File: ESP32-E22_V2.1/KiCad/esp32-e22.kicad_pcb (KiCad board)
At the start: 2 copper layers, 69.9 x 97.8 mm, 36 parts, among them J1 Conn_01x04_Socket, J10 Conn_01x02_Socket, J3 Conn_01x04_Socket, J4 Conn_01x03_Socket, J5 SMA, J6 Conn_01x02_Socket, J7 USB_C_Receptacle_PowerOnly_6P, J8 Conn_01x04_Socket, J9 Conn_01x02_Socket, SW1 SW_Push, U1 E22-40033S, U2 ESP32-DevKitC, U3 DM-OLED096-636

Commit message: new Version 2.0.10 & 2.0.6
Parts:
- removed J7: USB_C_Receptacle_PowerOnly_6P, Connector_USB:USB_C_Receptacle_GCT_USB4125-xx-x-0190_6P_TopMnt_Horizontal
- added J2: Conn_01x04_Socket, Connector_PinHeader_2.54mm:PinHeader_1x04_P2.54mm_Vertical, F.Cu at (158.8, 130.8)
- moved J8 47.4 mm to (123.2, 77.5), turned to 180 degrees
- moved D1 2.54 mm to (166.4, 119.4)
- moved R7 1.27 mm to (162.6, 104.1)
- moved R6 0.63 mm to (162.6, 107.3)
- moved REF** 0.32 mm to (175.6, 63.4)
- moved REF** 0.31 mm to (175.6, 138.4)
- moved REF** 0.07 mm to (115.6, 63.4)
- turned D2 to 180 degrees
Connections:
- D2 pad 1: GND -> +5V
- D2 pad 2: +5V -> GND
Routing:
- net /SDA: track 63.7 -> 121.9 mm
- net /SCL: track 57.0 -> 106.2 mm
- net +3.3V: track 135.9 -> 150.8 mm
- net Net-(D3-A): track 14.1 -> 4.87 mm
- net GND: track 417.2 -> 410.3 mm
- net +5V: track 113.6 -> 118.6 mm
- net Net-(J2-Pin_3): track 7.56 -> 8.83 mm
- net Net-(D1-A): track 7.62 -> 8.67 mm
- net /MISO: track 62.3 -> 63.1 mm
- net /E22_SCK: track 62.6 -> 63.3 mm
- net /E22_NSS: track 66.2 -> 66.9 mm
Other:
- board size 69.9 x 97.8 mm -> 70 x 99 mm

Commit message: real update
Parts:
- added C8: 100nF, Capacitor_THT:C_Disc_D4.7mm_W2.5mm_P5.00mm, F.Cu at (115.6, 75.0)
- added R8: 0R, Resistor_SMD:R_0805_2012Metric, B.Cu at (137.2, 55.4)
- J2: value Conn_01x04_Socket -> ~; footprint Connector_PinHeader_2.54mm:PinHeader_1x04_P2.54mm_Vertical -> footprints:USB-C_vert
- moved J2 3.17 mm to (161.9, 130.8), turned to 0 degrees
- moved D1 1.27 mm to (153.7, 125.7)
- renumbered C5 to C1, C6 to C2, C1 to C3, C2 to C4, C3 to C5, C7 to C6, C4 to C7, D3 to D1, D1 to D2, D2 to D3, J10 to J1, J9 to J3, J1 to J4, J4 to J5, J8 to J6, J3 to J7, J5 to J8, J6 to J9, R3 to R1, R4 to R2, R1 to R3, R2 to R4, U2 to U1, U3 to U2, U1 to U3
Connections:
- J8 pad 1: Net-(J5-In) -> Net-(J8-In)
- U3 pad 21: Net-(J5-In) -> Net-(U3-ANT)
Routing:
- net +3.3V: track 150.8 -> 159.5 mm
- net GND: track 410.3 -> 418.6 mm
- net /E22_DIO1: track 79.5 -> 72.8 mm
- net Net-(J5-In): track 6.64 -> 0.00 mm
- net /E22_BUSY: track 82.1 -> 76.9 mm
- net +5V: track 118.6 -> 122.4 mm
- net /E22_NRST: track 82.1 -> 78.4 mm
- net Net-(U3-ANT): track 0.00 -> 2.84 mm, vias 0 -> 1
- net Net-(J8-In): track 0.00 -> 2.39 mm
- net /MISO: track 63.1 -> 61.6 mm
- net Net-(D1-A): track 4.87 -> 5.87 mm
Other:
- board text added: "ESP32-E22 V2.1.0 designed by OE3WAS"

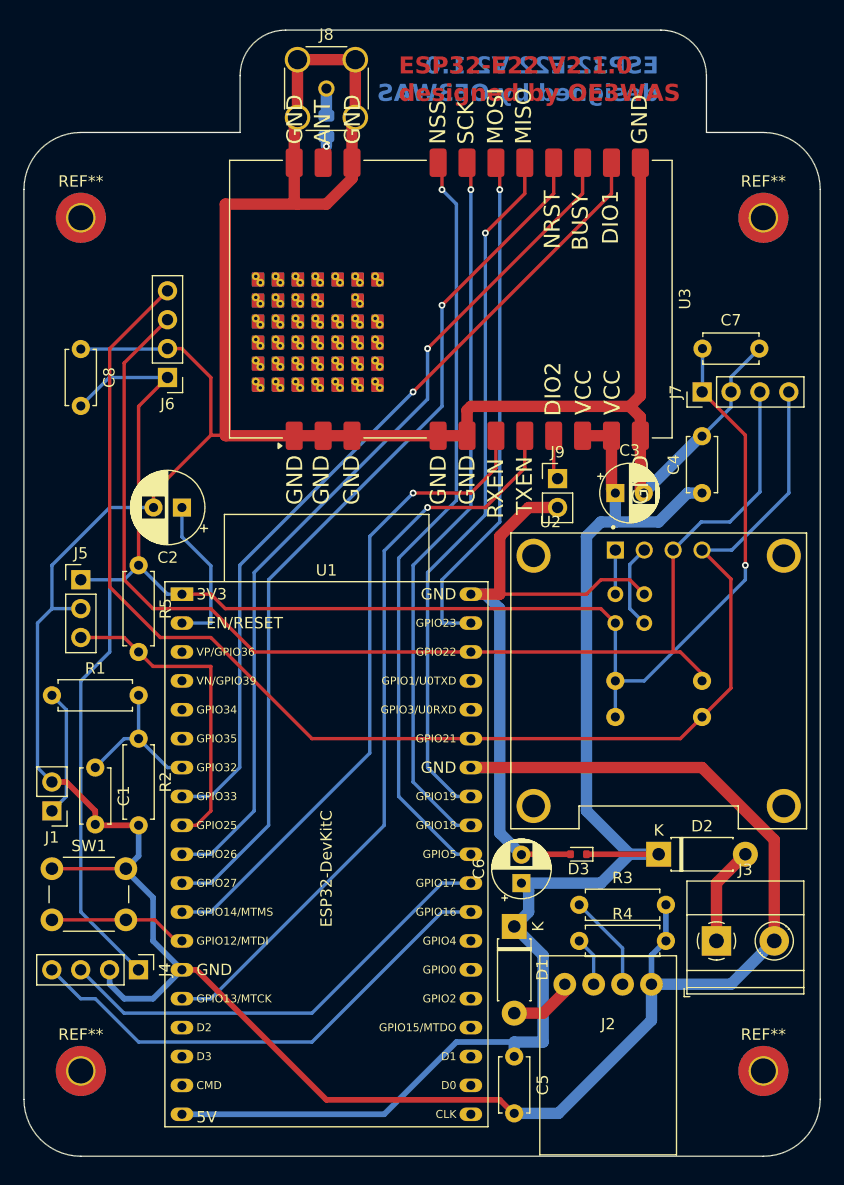
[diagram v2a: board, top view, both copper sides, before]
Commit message: Flood filled GND Back and Front
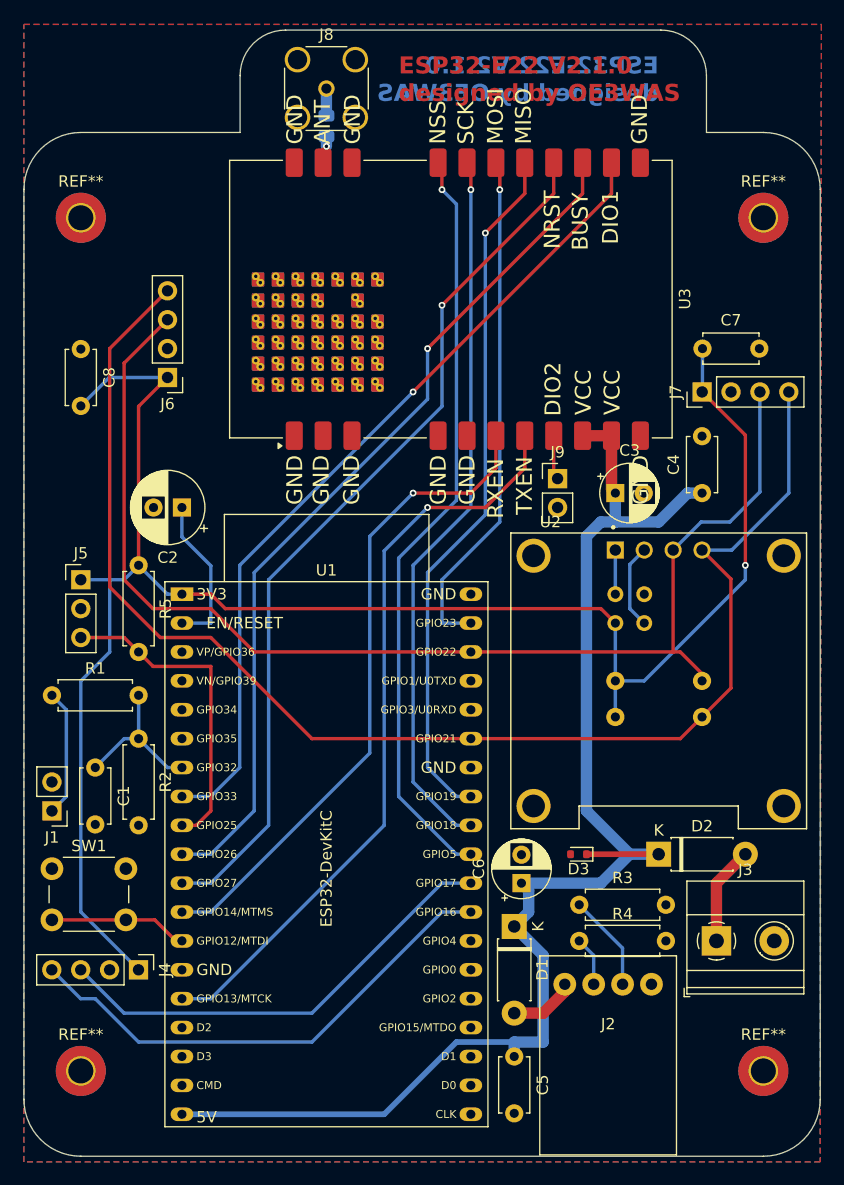
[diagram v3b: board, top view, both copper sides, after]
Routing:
- net GND: track 418.6 -> 0.00 mm
- added copper zone on B.Cu, net GND
- added copper zone on F.Cu, net GND

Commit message: some footprint changes
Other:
- board text added: "github.com/DK9BT/esp32-e22-lora-board"

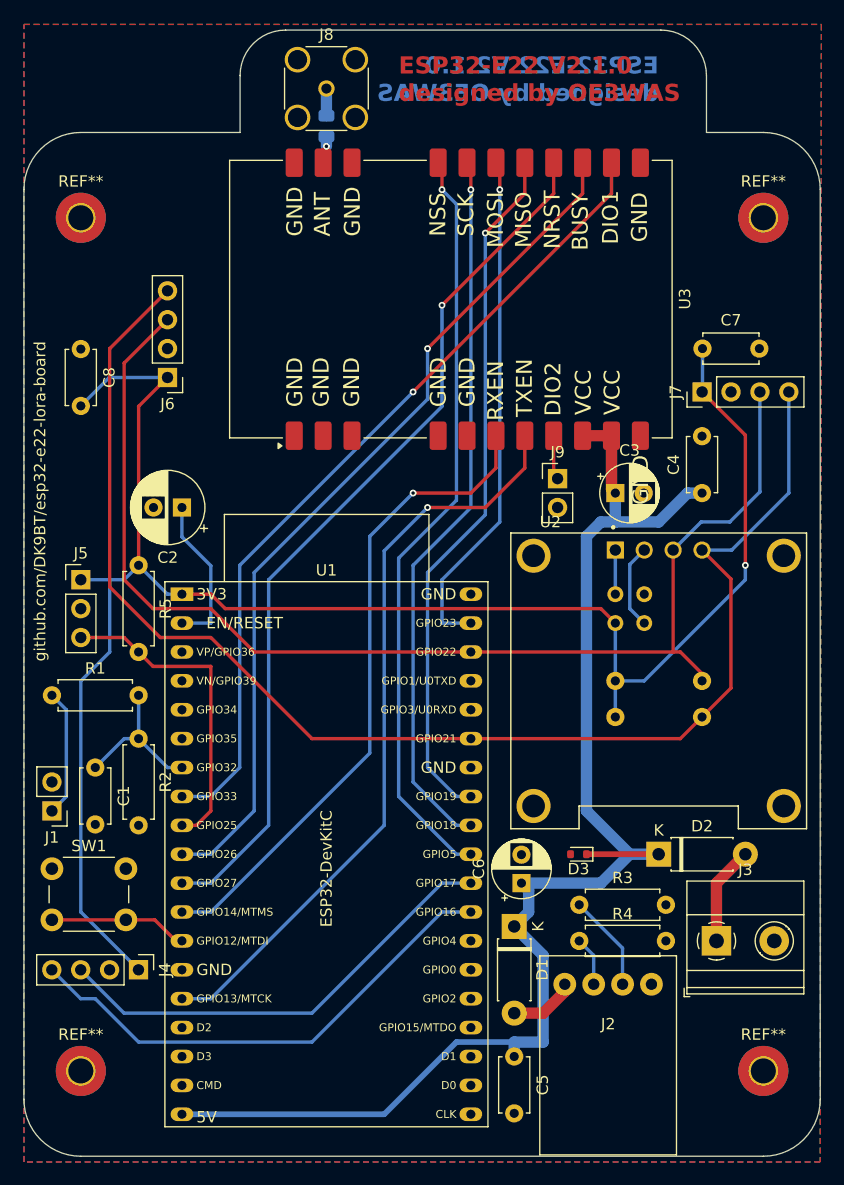
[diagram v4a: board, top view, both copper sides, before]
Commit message: corrected footprints symbols and 3d Models for our custom parts
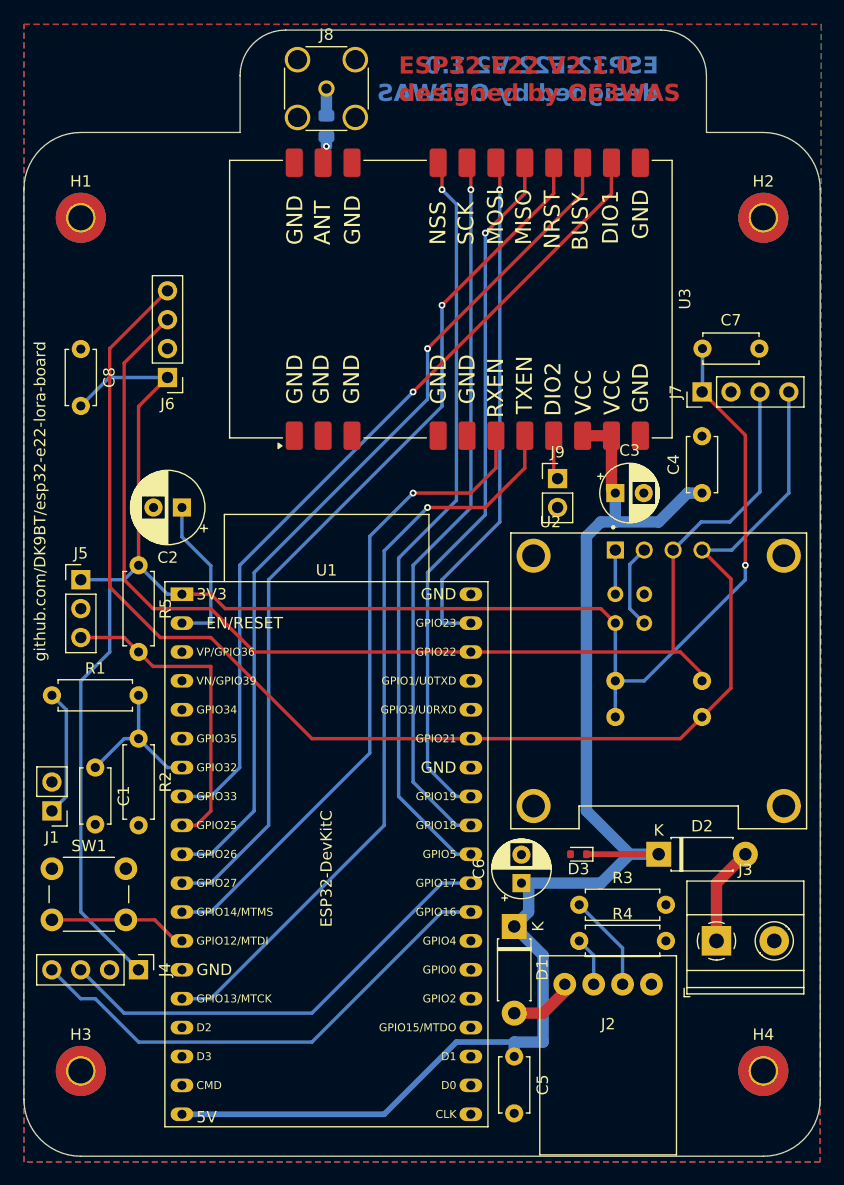
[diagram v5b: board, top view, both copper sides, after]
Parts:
- removed REF** (x4): MountingHole_2.2mm_M2_Pad_TopBottom, MountingHole:MountingHole_2.2mm_M2_Pad_TopBottom
- added H1: MountingHole_Pad, MountingHole:MountingHole_2.2mm_M2_Pad_TopBottom, F.Cu at (115.6, 63.4)
- added H2: MountingHole_Pad, MountingHole:MountingHole_2.2mm_M2_Pad_TopBottom, F.Cu at (175.6, 63.4)
- added H3: MountingHole_Pad, MountingHole:MountingHole_2.2mm_M2_Pad_TopBottom, F.Cu at (115.6, 138.4)
- added H4: MountingHole_Pad, MountingHole:MountingHole_2.2mm_M2_Pad_TopBottom, F.Cu at (175.6, 138.4)
- J2: footprint footprints:USB-C_vert -> footprints_local:USB-C_vert
- U1: footprint E22:ESP32-DevKitC -> footprints_local:ESP32-DevKitC
- U2: footprint E22:DM-OLED096-636 -> footprints_local:DM-OLED096-636
- U3: footprint E22:E22-400M33S -> footprints_local:E22-400M33S
